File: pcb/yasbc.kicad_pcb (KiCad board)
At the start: 4 copper layers, 207 parts, among them J1 USB TTY, J10 BOOT, J11 AudioJack3, J12 1V5, J13 VDDR, J14 3V3, J15 1V2, J2 ESP32 IO, J3 TTY_UART, J4 USB DEV, J5 Micro_SD_Card, J6 USB HOST, J7 GPIO, J9 SSD1306, Q1 AO3401A, Q2 AO3401A, U1 BCT2028, U2 BCT2028, U3 ESP32-WROOM-32, U4 Allwinner_A13, U5 CH340E, U6 TD6810, U7 SE5120, U8 K4B4G1646E, U9 MPU-6050, Y1 24M

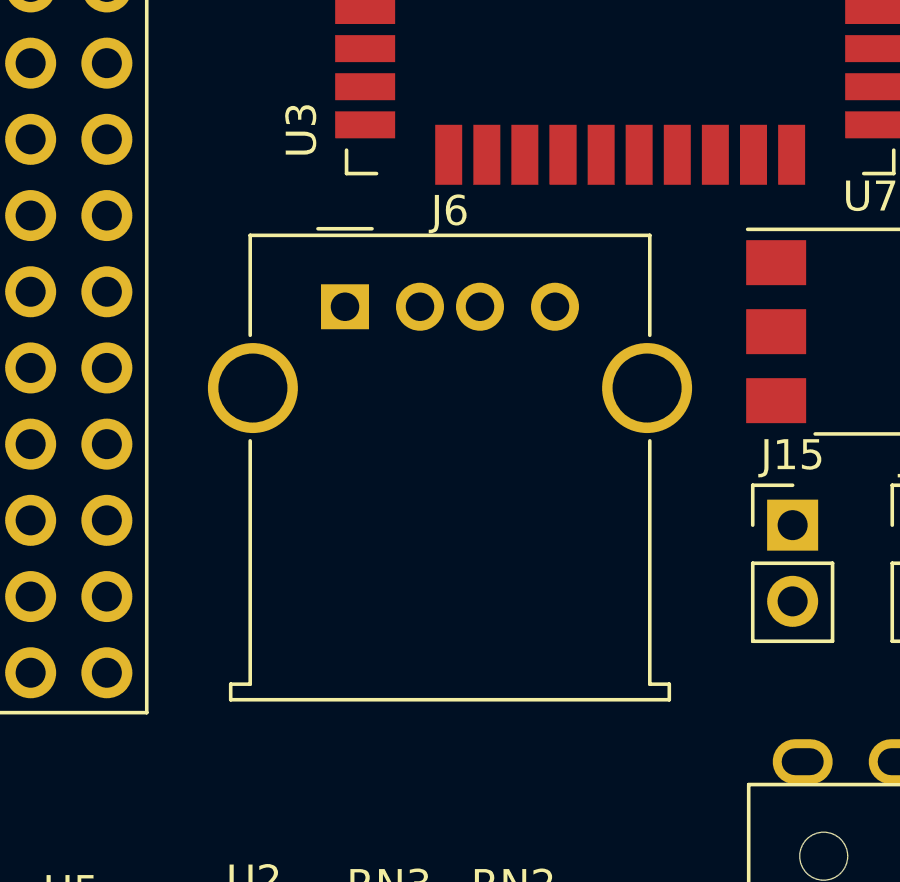
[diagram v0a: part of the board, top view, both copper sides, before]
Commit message: Added USB connector datasheets and footprints
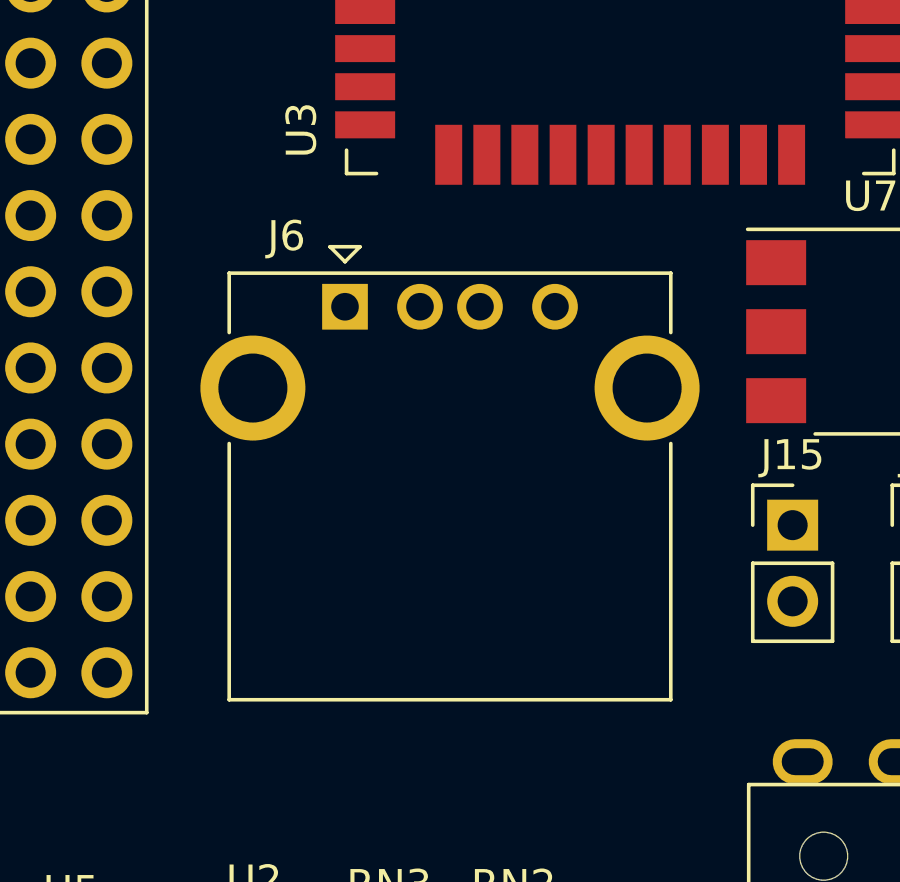
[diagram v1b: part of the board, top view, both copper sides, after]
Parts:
- J6: footprint Connector_USB:USB_A_Molex_67643_Horizontal -> Connector_USB:USB_A_CONNFLY_DS1095-WNR0

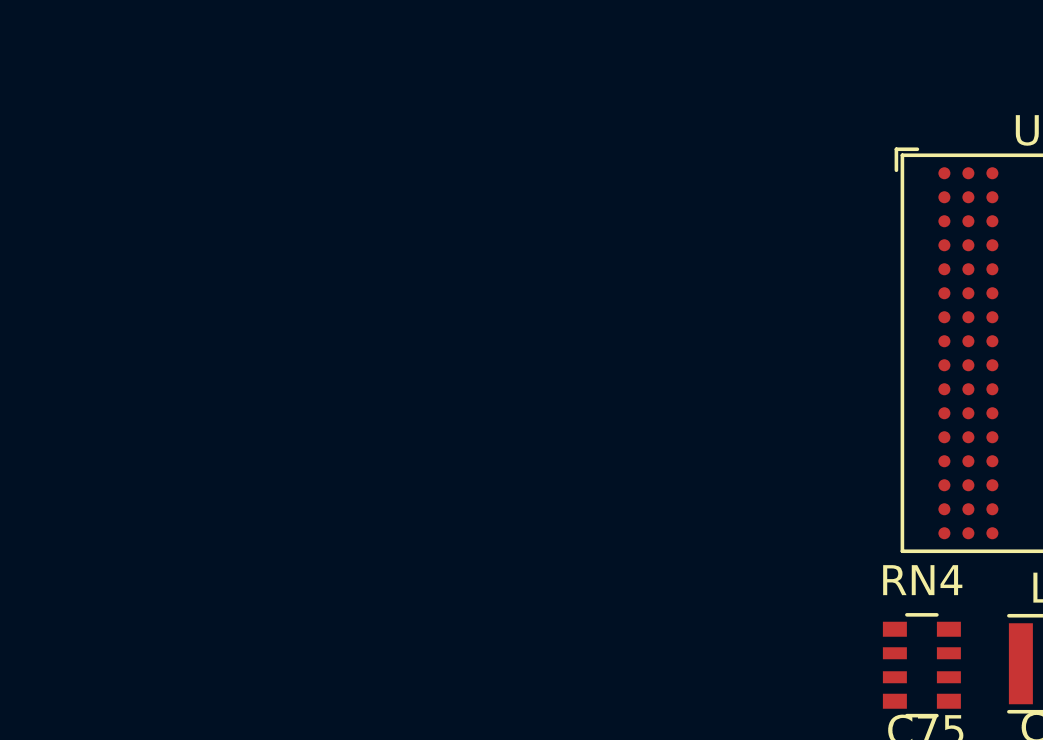
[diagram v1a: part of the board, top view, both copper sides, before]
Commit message: Added Reset and 5Way switch datasheets and footprints
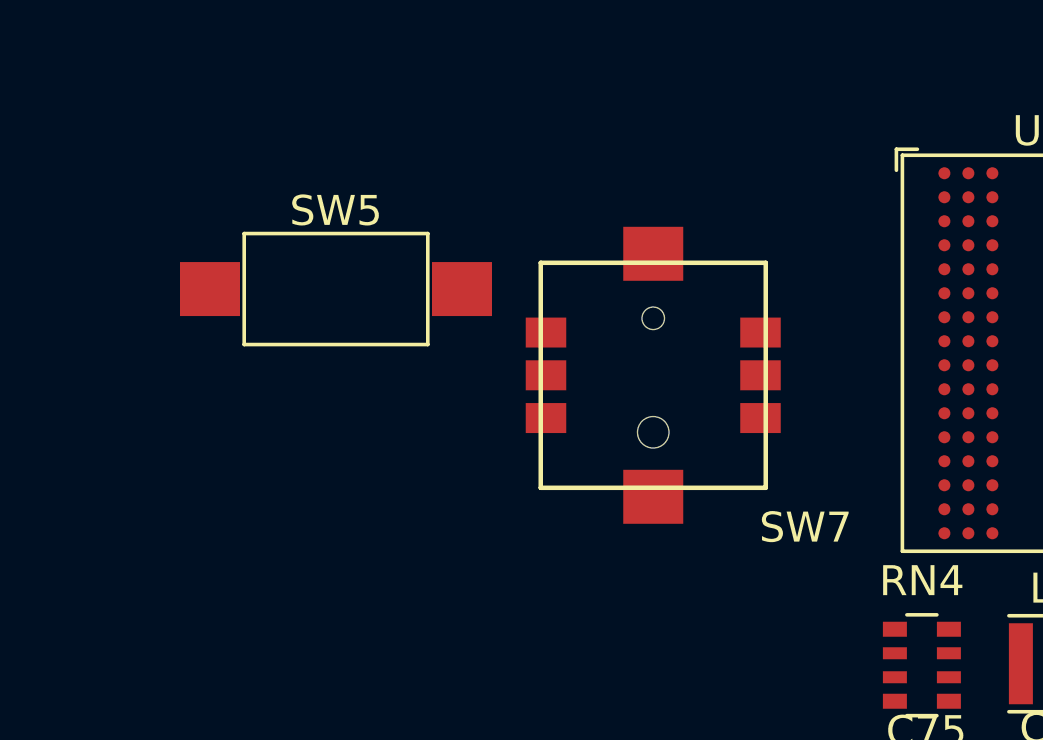
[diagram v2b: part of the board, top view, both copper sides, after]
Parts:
- added SW5: RESET, yasbc:HYP-1TS002B-2500-4300-CT, F.Cu at (-37.9, -30.6)
- added SW7: SW_5WAY, yasbc:Switches_ALPS-SKRHAAE010, F.Cu at (-27.3, -27.8)

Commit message: Added SPDT datasheets and footprints
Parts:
- added SW1: SW_SPDT, yasbc:SS-12D10, F.Cu at (38.8, -31.3)
- added SW2: SW_SPDT, yasbc:SS-12D10, F.Cu at (38.8, -23.2)
- added SW3: SW_SPDT, yasbc:SS-12D10, F.Cu at (53.1, -31.3)
- added SW4: SW_SPDT, yasbc:SS-12D10, F.Cu at (53.1, -23.2)

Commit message: Worked on layout
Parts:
- removed C46: 0.1u, Capacitor_SMD:C_0603_1608Metric
- removed J3: TTY_UART, Connector_PinHeader_2.54mm:PinHeader_1x03_P2.54mm_Vertical
- added TP1: TX, TestPoint:TestPoint_Pad_D2.0mm, F.Cu at (85.0, 121.5)
- added TP2: RX, TestPoint:TestPoint_Pad_D2.0mm, F.Cu at (85.0, 126.2)
- added TP3: GND, TestPoint:TestPoint_Pad_D2.0mm, F.Cu at (85.0, 131.0)
- C10, C11, C13, C15, C16, C18, C19, C20, C23, C24, C25, C28, C3, C30, C34, C35, C36, C37, C38, C39, C4, C41, C42, C43, C45, C47, C5, C50, C51, C53, C54, C56, C57, C58, C59, C8, C9, R11, R3, R4, R9, U3: moved to B.Cu
- C77, C78, C80, C81, C82, C83, C84, C85, C86, C87, C89, C90, C92, C93, C94, C97, C98, C99: footprint Capacitor_SMD:C_0603_1608Metric -> Capacitor_SMD:C_0402_1005Metric
- moved J15 350.8 mm to (264.3, 152.5), turned to 270 degrees
- moved U2 328.4 mm to (226.6, 156.6)
- moved U7 327.1 mm to (251.0, 123.2)
- moved L1 325.7 mm to (261.1, 156.3), turned to 90 degrees
- moved U6 324.1 mm to (265.5, 156.3)
- moved C55 317.0 mm to (258.3, 156.3), turned to 270 degrees
- moved J13 316.2 mm to (230.4, 152.6), turned to 270 degrees
- moved J12 315.2 mm to (247.8, 152.6), turned to 270 degrees
- moved C29 312.7 mm to (265.1, 159.1), turned to 180 degrees
- moved U3 312.5 mm to (237.4, 79.6), turned to 180 degrees
- moved U1 310.1 mm to (244.0, 156.6)
- moved R10 308.9 mm to (270.5, 156.3), turned to 270 degrees
- moved C32 308.8 mm to (268.7, 156.3), turned to 270 degrees
- moved C21 307.1 mm to (247.8, 157.6)
- moved C6 303.5 mm to (244.0, 159.6), turned to 180 degrees
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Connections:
- RN3 pad 1: /LED1 -> /LED3
- RN3 pad 2: /LED2 -> /LED1
- RN3 pad 3: /LED3 -> /LED2
- RN3 pad 6: Net-(D3-Pad2) -> Net-(D2-Pad2)
- RN3 pad 7: Net-(D2-Pad2) -> Net-(D1-Pad2)
- RN3 pad 8: Net-(D1-Pad2) -> Net-(D3-Pad2)
- RN4 pad 1: /LED5 -> Net-(D6-Pad2)
- RN4 pad 2: /LED6 -> Net-(D8-Pad2)
- RN4 pad 3: /LED7 -> Net-(D7-Pad2)
- RN4 pad 4: /LED8 -> Net-(D5-Pad2)
- RN4 pad 5: Net-(D8-Pad2) -> /LED5
- RN4 pad 6: Net-(D7-Pad2) -> /LED7
- RN4 pad 7: Net-(D6-Pad2) -> /LED8
- RN4 pad 8: Net-(D5-Pad2) -> /LED6
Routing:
- net Net-(J11-PadS): track 0.00 -> 18.8 mm
- net GND: track 0.00 -> 17.0 mm, vias 0 -> 19
- net VBUS: track 0.00 -> 16.5 mm
- net Net-(J11-PadT): track 0.00 -> 13.6 mm
- net Net-(C55-Pad1): track 0.00 -> 11.3 mm
- net +3V3: track 0.00 -> 10.9 mm
- net Net-(D5-Pad2): track 0.00 -> 10.4 mm
- net Net-(D4-Pad2): track 0.00 -> 10.3 mm
- net Net-(J11-PadR): track 0.00 -> 9.85 mm
- net Net-(J1-PadA7): track 0.00 -> 9.77 mm
- net Net-(J1-PadA6): track 0.00 -> 7.90 mm
- net Net-(J4-PadA5): track 0.00 -> 7.84 mm
- net Net-(J1-PadA5): track 0.00 -> 7.84 mm
- net Net-(J1-PadB5): track 0.00 -> 7.59 mm
- net Net-(J4-PadB5): track 0.00 -> 7.59 mm
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
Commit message: Added boost reg for OLED and new inductors
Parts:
- added C106: 10u, Capacitor_SMD:C_0603_1608Metric, F.Cu at (206.0, 158.0)
- added C46: 10u, Capacitor_SMD:C_0603_1608Metric, F.Cu at (202.0, 158.0)
- added L2: 4.7u, Inductor_SMD:L_0805_2012Metric_Pad1.15x1.40mm_HandSolder, F.Cu at (207.2, 154.4)
- added R65: 10K, Resistor_SMD:R_0603_1608Metric, F.Cu at (211.5, 153.3)
- added R66: 200K, Resistor_SMD:R_0603_1608Metric, F.Cu at (210.0, 158.0)
- added U10: MT3608, Package_TO_SOT_SMD:SOT-23-6, F.Cu at (202.4, 154.4)
- L1: footprint yasbc:Inductor_SMD_3x3mm -> Inductor_SMD:L_1008_2520Metric
- moved C64 235.2 mm to (159.9, 157.3)
- moved R63 232.0 mm to (155.0, 160.8)
- moved R56 228.8 mm to (154.6, 157.0)
- moved C65 227.7 mm to (158.2, 152.0)
- moved R55 216.4 mm to (149.0, 147.0)
- moved R12 214.7 mm to (149.0, 150.8)
- moved R54 214.4 mm to (144.0, 150.2)
- moved C103 211.8 mm to (152.8, 150.8)
- moved R59 211.4 mm to (144.0, 146.0)
- moved C66 208.4 mm to (155.6, 145.7)
- moved C68 208.4 mm to (159.6, 143.2)
- moved D1 135.5 mm to (110.8, 147.6)
- moved D2 135.5 mm to (112.8, 147.6)
- moved D3 135.5 mm to (114.8, 147.6)
- moved D4 135.5 mm to (116.8, 147.6)
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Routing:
- net GND: track 17.0 -> 26.9 mm, vias 19 -> 11
- net Net-(C26-Pad1): track 0.00 -> 3.12 mm
- net VBUS: track 16.5 -> 14.1 mm
- net Net-(C6-Pad1): track 1.95 -> 4.13 mm
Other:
- board text added: "OLED"

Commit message: Added new OLED, worked on sch & pcb
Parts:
- removed the C104 at (182.7, 72.6)
- removed C106: 10u, Capacitor_SMD:C_0603_1608Metric
- removed the C26 at (247.8, 155.6)
- removed the C46 at (202.0, 158.0)
- removed the C55 at (258.2, 155.9)
- removed the C63 at (125.0, 77.6)
- removed the C70 at (120.1, 28.5)
- removed the C71 at (122.6, 28.5)
- removed the C95 at (179.5, 71.0)
- removed the C96 at (182.7, 71.0)
- removed the J2 at (-43.4, -9.74)
- removed the J7 at (-80.1, -34.2)
- removed the R16 at (-17.9, 14.7)
- removed the R17 at (6.98, -10.0)
- removed the R18 at (-6.70, 3.79)
- removed the R19 at (15.0, -17.6)
- removed the R23 at (-10.7, 1.28)
- removed the R24 at (10.6, -20.1)
- removed the R25 at (-25.9, 17.2)
- removed the R26 at (-1.08, -7.74)
- removed the R29 at (-3.77, 6.30)
- removed the R30 at (-13.9, 17.2)
- removed the R31 at (-8.77, 12.2)
- removed the R35 at (-18.1, 22.2)
- removed the R36 at (-4.76, 8.81)
- removed R40, R41: 22, Resistor_SMD:R_0603_1608Metric
- removed R42, R51: 240 1%, Resistor_SMD:R_0603_1608Metric
- removed R43, R44, R52, R53: 2K, Resistor_SMD:R_0603_1608Metric
- removed R45: 47K, Resistor_SMD:R_0603_1608Metric
- removed R47, R48: 100, Resistor_SMD:R_0603_1608Metric
- removed R57, R58: 5.1K, Resistor_SMD:R_0603_1608Metric
- removed the U10 at (202.4, 154.4)
- added C100: 0.1u, Capacitor_SMD:C_0603_1608Metric, F.Cu at (143.3, 122.2)
- added C101: 0.1u, Capacitor_SMD:C_0603_1608Metric, F.Cu at (140.1, 120.6)
- added C102: 0.1u, Capacitor_SMD:C_0603_1608Metric, F.Cu at (143.3, 120.6)
- added C28: 0.1u, Capacitor_SMD:C_0603_1608Metric, F.Cu at (247.5, 155.5)
- added C48: 10u, Capacitor_SMD:C_0603_1608Metric, F.Cu at (259.5, 155.9)
- added C65: 10u, Capacitor_SMD:C_0603_1608Metric, F.Cu at (198.0, 154.4)
- added C66: 0.1u, Capacitor_SMD:C_0603_1608Metric, F.Cu at (121.8, 77.6)
- added D1: D_Schottky, Diode_SMD:D_SOD-323, F.Cu at (198.9, 151.8)
- added U9: K4B4G1646E, Package_BGA:BGA-96_9.0x13.0mm_Layout2x3x16_P0.8mm, F.Cu at (106.6, 100.7)
- C62: value 0.1u -> 10u
- C67: value 10u -> 0.1u
- C72: value 1u -> 10u
- J11: renamed from J9; value SSD1306 -> SSD1309; footprint yasbc:SSD1306 -> yasbc:SSD1309
- R20, R37: value 22 -> 240 1%
- R21, R22, R38, R39: value 22 -> 2K
- R27, R28: value 22 -> 5.1K
- R31: renamed from R46; value 400K -> 960K
- R32, R33: value 22 -> 100
- R34: value 22 -> 47K
- U8: value K4B4G1646E -> MT3608; footprint Package_BGA:BGA-96_9.0x13.0mm_Layout2x3x16_P0.8mm -> Package_TO_SOT_SMD:SOT-23-6
- moved R39 190.1 mm to (143.3, 119.0)
- moved R37 183.6 mm to (140.1, 122.2)
- moved R38 182.2 mm to (140.1, 119.0)
- moved C67 156.6 mm to (125.0, 77.6)
- moved R22 150.6 mm to (125.0, 76.0)
- moved R21 144.0 mm to (121.8, 76.0)
- moved R20 142.6 mm to (125.0, 74.4)
- moved C62 111.7 mm to (205.1, 152.0), turned to 270 degrees
- moved C72 110.2 mm to (15.6, 16.4), turned to 0 degrees
- moved U8 86.0 mm to (202.4, 154.4)
- moved C82 67.7 mm to (122.3, 119.8)
- moved C83 67.7 mm to (122.3, 121.4)
- moved C91 67.7 mm to (122.3, 123.0)
- moved C97 67.7 mm to (122.3, 124.6)
- moved C103 67.7 mm to (131.9, 124.6)
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- renumbered C97 to C103, C98 to C104, C99 to C105, C15 to C14, C16 to C15, C17 to C16, C18 to C17, C19 to C18, C20 to C19, C14 to C20, C100 to C23, C23 to C24, C24 to C25, C25 to C26, C101 to C27, C27 to C29, C102 to C30, C33 to C31, C28 to C32, C29 to C33, C30 to C34, C31 to C35, C32 to C36, C34 to C37, C35 to C38, C36 to C39, C37 to C40, C38 to C41, C39 to C42, C40 to C43, C41 to C44, C42 to C45, C43 to C46, C44 to C47, C45 to C49, C47 to C50, C48 to C51, C49 to C52, C50 to C53, C51 to C54, C52 to C55, C53 to C56, C54 to C57, C56 to C58, C57 to C59, C58 to C60, C59 to C61, C60 to C63, C61 to C64, C103 to C68, C64 to C69, C65 to C70, C66 to C71, C69 to C73, C68 to C74, C73 to C78, C74 to C79, C75 to C80, C76 to C81, C77 to C82, C78 to C83, C79 to C84, C80 to C85, C81 to C86, C82 to C87, C83 to C88, C84 to C89, C85 to C90, C86 to C91, C87 to C92, C88 to C93, C89 to C94, C90 to C95, C91 to C96, C92 to C97, C93 to C98, C94 to C99, D3 to D2, D1 to D3, D2 to D4, D4 to D5, D8 to D7, D7 to D8, D5 to D9, J10 to J1, J6 to J10, J1 to J2, J11 to J3, J12 to J4, J13 to J5, J14 to J6, J15 to J7, J4 to J8, J5 to J9, R61 to R10, R62 to R11, R9 to R12, R10 to R13, R11 to R14, R13 to R15, R14 to R16, R15 to R17, R66 to R18, R65 to R19, R12 to R23, R54 to R24, R55 to R25, R56 to R26, R59 to R29, R8 to R3, R63 to R30, R49 to R35, R50 to R36, R3 to R4, R4 to R5, R5 to R6, R60 to R8, R6 to R9, RN2 to RN1, RN3 to RN2, RN4 to RN3, RN5 to RN4, SW5 to SW1, SW4 to SW2, SW2 to SW4, SW1 to SW5, SW7 to SW6, U9 to U10
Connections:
- net /USB_DEV_DM renamed /USB_DEV_D-
- net /USB_DEV_DP renamed /USB_DEV_D+
- net /USB_HOST_DM renamed /USB_HOST_D-
- net /USB_HOST_DP renamed /USB_HOST_D+
- C62 pad 1: +1V5 -> VBUS
- C62 pad 2: Net-(C62-Pad2) -> GND
- C67 pad 1: /SW_CENTER -> Net-(C66-Pad2)
- C72 pad 1: +3V3 -> /SW_CENTER
- C73 pad 1: Net-(C69-Pad1) -> Net-(C73-Pad1)
- C79 pad 1: Net-(C74-Pad1) -> +12V
- J11 pad 10: GND -> Net-(J11-Pad10)
- J11 pad 11: GND -> /OLED_SDIN
- J11 pad 12: GND -> /OLED_SCLK
- J11 pad 13: /OLED_CS -> GND
- J11 pad 14: /OLED_RES -> GND
- J11 pad 16: GND -> /OLED_RES
- J11 pad 17: GND -> /OLED_CS
- J11 pad 18: /OLED_SCLK -> Net-(J11-Pad18)
- J11 pad 19: /OLED_SDIN -> GND
- J11 pad 2: Net-(C70-Pad1) -> +12V
- J11 pad 20: Net-(J9-Pad20) -> GND
- J11 pad 21: GND -> +3V3
- J11 pad 22: GND -> Net-(J11-Pad22)
- J11 pad 23: GND -> Net-(J11-Pad23)
- J11 pad 24: GND -> Net-(J11-Pad24)
- J11 pad 25: GND -> Net-(J11-Pad25)
- J11 pad 26: Net-(J9-Pad26) -> Net-(J11-Pad26)
- J11 pad 27: Net-(C69-Pad1) -> Net-(J11-Pad27)
- J11 pad 28: Net-(C74-Pad1) -> Net-(J11-Pad28)
- J11 pad 29: GND -> Net-(J11-Pad29)
- J11 pad 3: Net-(C70-Pad2) -> Net-(C73-Pad1)
- J11 pad 4: Net-(C71-Pad1) -> Net-(J11-Pad4)
- J11 pad 5: Net-(C71-Pad2) -> GND
- J11 pad 6: +3V3 -> GND
- J11 pad 7: Net-(J9-Pad7) -> GND
- J11 pad 9: +3V3 -> GND
- L2 pad 2: Net-(D9-Pad2) (its old number) -> Net-(D1-Pad2)
- R18 pad 2: Net-(R65-Pad2) -> Net-(R18-Pad2)
- R19 pad 2: Net-(R65-Pad2) -> Net-(R18-Pad2)
- R20 pad 2: /DDR3_CKN -> GND
- R21 pad 1: Net-(R21-Pad1) -> +1V5
- R21 pad 2: /DDR3_CKE -> Net-(C66-Pad2)
- R22 pad 1: Net-(R22-Pad1) -> Net-(C66-Pad2)
- R22 pad 2: /DDR3_RST -> GND
- R24 pad 1: Net-(R54-Pad1) -> Net-(R24-Pad1)
- R25 pad 1: Net-(R55-Pad1) -> Net-(R25-Pad1)
- R27 pad 1: Net-(R27-Pad1) -> Net-(R24-Pad1)
- R27 pad 2: /DDR3_A0 -> /SW_R2R
- R28 pad 1: Net-(R28-Pad1) -> Net-(R25-Pad1)
- R28 pad 2: /DDR3_A1 -> Net-(R24-Pad1)
- R29 pad 2: Net-(R55-Pad1) -> Net-(R25-Pad1)
- R31 pad 1: Net-(J9-Pad26) -> Net-(J11-Pad4)
- R32 pad 2: /DDR3_A5 -> /TTY_TX
- R33 pad 2: /DDR3_A6 -> /TTY_RX
- R34 pad 1: Net-(R34-Pad1) -> /SW_LEFT
- R34 pad 2: /DDR3_A7 -> GND
- R37 pad 2: /DDR3_A10 -> GND
- R38 pad 1: Net-(R38-Pad1) -> VDDR
- R38 pad 2: /DDR3_A11 -> Net-(C101-Pad2)
- R39 pad 1: Net-(R39-Pad1) -> Net-(C101-Pad2)
- R39 pad 2: /DDR3_A12 -> GND
- RN4 pad 5: /SW_DOWN -> /SW_CENTER
- RN4 pad 6: /SW_CENTER -> /SW_RIGHT
- RN4 pad 7: /SW_RIGHT -> /SW_UP
- RN4 pad 8: /SW_UP -> /SW_DOWN
- U3 pad 10: /IO25 -> Net-(U3-Pad10)
- U3 pad 11: /IO26 -> Net-(U3-Pad11)
- U3 pad 12: /IO27 -> Net-(U3-Pad12)
- U3 pad 27: /IO16 -> Net-(U3-Pad27)
- U3 pad 28: /IO17 -> Net-(U3-Pad28)
- U3 pad 29: /IO5 -> Net-(U3-Pad29)
- U3 pad 30: /IO18 -> Net-(U3-Pad30)
- U3 pad 33: /IO21 -> Net-(U3-Pad33)
- U3 pad 37: /IO23 -> Net-(U3-Pad37)
- U3 pad 6: /IO34 -> Net-(U3-Pad6)
- U3 pad 7: /IO35 -> Net-(U3-Pad7)
- U3 pad 8: /IO32 -> Net-(U3-Pad8)
- U3 pad 9: /IO33 -> Net-(U3-Pad9)
- U4 pad 114: /CSI_PCLK -> Net-(U4-Pad114)
- U4 pad 115: /CSI_MCLK -> Net-(U4-Pad115)
- U4 pad 116: /CSI_HSYNC -> Net-(U4-Pad116)
- U4 pad 117: /CSI_VSYNC -> Net-(U4-Pad117)
- U4 pad 118: /CSI_D0 -> Net-(U4-Pad118)
- U4 pad 119: /CSI_D1 -> Net-(U4-Pad119)
- U4 pad 120: /CSI_D2 -> Net-(U4-Pad120)
- U4 pad 121: /CSI_D3 -> Net-(U4-Pad121)
- U4 pad 122: /CSI_D4 -> Net-(U4-Pad122)
- U4 pad 123: /CSI_D5 -> Net-(U4-Pad123)
- U4 pad 124: /CSI_D6 -> Net-(U4-Pad124)
- U4 pad 125: /CSI_D7 -> Net-(U4-Pad125)
- U4 pad 126: /LCD_VSYNC -> Net-(U4-Pad126)
- U4 pad 127: /LCD_HSYNC -> Net-(U4-Pad127)
- U4 pad 128: /LCD_DE -> Net-(U4-Pad128)
- U4 pad 129: /LCD_CLK -> Net-(U4-Pad129)
- U4 pad 130: /LCD_D23 -> Net-(U4-Pad130)
- U4 pad 131: /LCD_D22 -> Net-(U4-Pad131)
- U4 pad 132: /LCD_D21 -> Net-(U4-Pad132)
- U4 pad 133: /LCD_D20 -> Net-(U4-Pad133)
- U4 pad 134: /LCD_D19 -> Net-(U4-Pad134)
- U4 pad 135: /LCD_D18 -> Net-(U4-Pad135)
- U4 pad 136: /LCD_D15 -> Net-(U4-Pad136)
- U4 pad 137: /LCD_D14 -> Net-(U4-Pad137)
- U4 pad 138: /LCD_D13 -> Net-(U4-Pad138)
- U4 pad 139: /LCD_D12 -> Net-(U4-Pad139)
- U4 pad 140: /LCD_D11 -> Net-(U4-Pad140)
- U4 pad 141: /LCD_D10 -> Net-(U4-Pad141)
- U4 pad 143: /LCD_D7 -> Net-(U4-Pad143)
- U4 pad 144: /LCD_D6 -> Net-(U4-Pad144)
- U4 pad 145: /LCD_D5 -> Net-(U4-Pad145)
- U4 pad 146: /LCD_D4 -> Net-(U4-Pad146)
- U4 pad 147: /LCD_D3 -> Net-(U4-Pad147)
- U4 pad 148: /LCD_D2 -> Net-(U4-Pad148)
- U4 pad 151: Net-(R48-Pad1) -> Net-(R33-Pad1)
- U4 pad 152: Net-(R47-Pad1) -> Net-(R32-Pad1)
- U4 pad 17: Net-(R42-Pad1) -> Net-(R20-Pad1)
- U4 pad 18: Net-(C62-Pad2) -> Net-(C66-Pad2)
- U4 pad 31: /DDR3_DQS0 -> /DDR3_DQS0+
- U4 pad 32: /DDR3_DQS0N -> /DDR3_DQS0-
- U4 pad 33: /DDR3_DQS1 -> /DDR3_DQS1+
- U4 pad 34: /DDR3_DQS1N -> /DDR3_DQS1-
- U4 pad 45: Net-(R19-Pad1) -> /DDR3_CK+
- U4 pad 46: Net-(R20-Pad1) -> /DDR3_CK-
- U4 pad 47: Net-(R21-Pad1) -> /DDR3_CKE
- U4 pad 48: Net-(R37-Pad1) -> /DDR3_A10
- U4 pad 49: Net-(R17-Pad1) -> /DDR3_BA1
- U4 pad 50: Net-(R39-Pad1) -> /DDR3_A12
- U4 pad 51: Net-(R31-Pad1) -> /DDR3_A4
- U4 pad 52: Net-(R28-Pad1) -> /DDR3_A1
- U4 pad 54: Net-(R33-Pad1) -> /DDR3_A6
- U4 pad 55: Net-(R35-Pad1) -> /DDR3_A8
- U4 pad 56: Net-(R38-Pad1) -> /DDR3_A11
- U4 pad 57: Net-(R41-Pad1) -> /DDR3_A14
- U4 pad 58: Net-(R24-Pad1) -> /DDR3_RAS
- U4 pad 59: Net-(R23-Pad1) -> /DDR3_CAS
- U4 pad 60: Net-(R25-Pad1) -> /DDR3_WE
- U4 pad 61: Net-(R18-Pad1) -> /DDR3_BA2
- U4 pad 63: Net-(R16-Pad1) -> /DDR3_BA0
- U4 pad 64: Net-(R27-Pad1) -> /DDR3_A0
- U4 pad 65: Net-(R30-Pad1) -> /DDR3_A3
- U4 pad 66: Net-(R29-Pad1) -> /DDR3_A2
- U4 pad 67: Net-(R32-Pad1) -> /DDR3_A5
- U4 pad 68: Net-(R40-Pad1) -> /DDR3_A13
- U4 pad 69: Net-(R36-Pad1) -> /DDR3_A9
- U4 pad 70: Net-(R22-Pad1) -> /DDR3_RST
- U4 pad 71: Net-(R34-Pad1) -> /DDR3_A7
- U4 pad 72: Net-(R26-Pad1) (its old number) -> /DDR3_ODT
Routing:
- net GND: track 26.9 -> 46.4 mm, vias 11 -> 6
- net /DDR3_D5: track 0.00 -> 10.4 mm
- net /DDR3_D7: track 0.00 -> 9.78 mm
- net /DDR3_D4: track 0.00 -> 9.16 mm
- net /DDR3_D6: track 0.00 -> 8.99 mm
- net /DDR3_D3: track 0.00 -> 8.72 mm
- net /DDR3_DQS0-: track 0.00 -> 8.49 mm
- net /DDR3_D1: track 0.00 -> 8.12 mm
- net /DDR3_D2: track 0.00 -> 8.11 mm
- net /DDR3_DQS0+: track 0.00 -> 7.68 mm
- net VBUS: track 14.1 -> 21.7 mm
- net /DDR3_DM0: track 0.00 -> 7.33 mm
- net /DDR3_D0: track 0.00 -> 6.91 mm
- net Net-(C95-Pad2): track 6.44 -> 0.00 mm
- net Net-(C101-Pad2): track 0.00 -> 6.44 mm
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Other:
- net class Default: clearance 0.1524 -> 0.1016; via_dia 0.4064 -> 0.4572
- net class HighSpeed added: clearance 0.1016, trace_width 0.2032, via_dia 0.4572, via_drill 0.2032
- rule trace_clearance: 0.1524 -> 0.1016
- rule trace_min: 0.127 -> 0.1016
- rule via_min_size: 0.4 -> 0.45
- board text removed: "OLED"

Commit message: Reduced to one +1V5 LDO
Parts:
- removed the C2 at (223.1, 155.6)
- removed the C22 at (230.1, 157.7)
- removed the C29 at (230.1, 155.5)
- removed the C7 at (226.6, 159.3)
- removed the J5 at (230.4, 152.6)
- removed the R2 at (223.1, 157.6)
- removed the U2 at (226.6, 156.6)
- C1: value 0.1u -> 1u
- C25: renamed from C28; value 0.1u -> 1u
- renumbered C12 to C10, C13 to C11, C14 to C12, C15 to C13, C16 to C14, C17 to C15, C18 to C16, C19 to C17, C20 to C18, C21 to C19, C3 to C2, C23 to C20, C24 to C21, C25 to C22, C26 to C23, C27 to C24, C30 to C26, C31 to C27, C32 to C28, C33 to C29, C4 to C3, C34 to C30, C35 to C31, C36 to C32, C37 to C33, C38 to C34, C39 to C35, C40 to C36, C41 to C37, C42 to C38, C43 to C39, C5 to C4, C44 to C40, C45 to C41, C46 to C42, C47 to C43, C48 to C44, C49 to C45, C50 to C46, C51 to C47, C52 to C48, C53 to C49, C6 to C5, C54 to C50, C55 to C51, C56 to C52, C57 to C53, C58 to C54, C59 to C55, C60 to C56, C61 to C57, C62 to C58, C63 to C59, C8 to C6, C64 to C60, C65 to C61, C66 to C62, C67 to C63, C68 to C64, C69 to C65, C70 to C66, C71 to C67, C72 to C68, C74 to C69, C9 to C7, C80 to C70, C82 to C71, C81 to C72, C83 to C73, C84 to C74, C73 to C75, C85 to C76, C86 to C77, C79 to C78, C78 to C79, C10 to C8, C87 to C80, C88 to C81, C89 to C82, C90 to C83, C91 to C84, C92 to C85, C94 to C86, C93 to C87, C95 to C88, C96 to C89, C11 to C9, C97 to C90, C98 to C91, C99 to C92, C100 to C93, C101 to C94, C102 to C95, C103 to C96, C104 to C97, C105 to C98, J11 to J10, J6 to J5, J7 to J6, J8 to J7, J9 to J8, J10 to J9, R11 to R10, R12 to R11, R13 to R12, R14 to R13, R15 to R14, R16 to R15, R17 to R16, R18 to R17, R19 to R18, R20 to R19, R3 to R2, R21 to R20, R22 to R21, R23 to R22, R24 to R23, R25 to R24, R26 to R25, R27 to R26, R28 to R27, R29 to R28, R30 to R29, R4 to R3, R32 to R30, R33 to R31, R34 to R32, R35 to R33, R36 to R34, R31 to R35, R37 to R36, R38 to R37, R39 to R38, R5 to R4, R6 to R5, R7 to R6, R8 to R7, R9 to R8, R10 to R9, U3 to U2, U4 to U3, U5 to U4, U6 to U5, U7 to U6, U8 to U7, U9 to U8, U10 to U9
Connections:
- C70 pad 1: VDDR -> +1V5
- C71 pad 1: VDDR -> +1V5
- C73 pad 1: VDDR -> +1V5
- C76 pad 1: VDDR -> +1V5
- C77 pad 1: VDDR -> +1V5
- C80 pad 1: VDDR -> +1V5
- C81 pad 1: VDDR -> +1V5
- C82 pad 1: VDDR -> +1V5
- C83 pad 1: VDDR -> +1V5
- C84 pad 1: VDDR -> +1V5
- C85 pad 1: VDDR -> +1V5
- C86 pad 1: VDDR -> +1V5
- C88 pad 1: VDDR -> +1V5
- C90 pad 1: VDDR -> +1V5
- C91 pad 1: VDDR -> +1V5
- C92 pad 1: VDDR -> +1V5
- C94 pad 1: VDDR -> +1V5
- C96 pad 1: VDDR -> +1V5
- C97 pad 1: VDDR -> +1V5
- C98 pad 1: VDDR -> +1V5
- R37 pad 1: VDDR -> +1V5
- U8 pad A1: VDDR -> +1V5
- U8 pad A8: VDDR -> +1V5
- U8 pad B2: VDDR -> +1V5
- U8 pad C1: VDDR -> +1V5
- U8 pad C9: VDDR -> +1V5
- U8 pad D2: VDDR -> +1V5
- U8 pad D9: VDDR -> +1V5
- U8 pad E9: VDDR -> +1V5
- U8 pad F1: VDDR -> +1V5
- U8 pad G7: VDDR -> +1V5
- U8 pad H2: VDDR -> +1V5
- U8 pad H9: VDDR -> +1V5
- U8 pad K2: VDDR -> +1V5
- U8 pad K8: VDDR -> +1V5
- U8 pad N1: VDDR -> +1V5
- U8 pad N9: VDDR -> +1V5
- U8 pad R1: VDDR -> +1V5
- U8 pad R9: VDDR -> +1V5
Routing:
- net GND: track 46.4 -> 38.8 mm
- net VBUS: track 21.7 -> 16.9 mm
- net Net-(C29-Pad1): track 4.54 -> 0.00 mm
- net Net-(C7-Pad1): track 3.48 -> 0.00 mm
- net Net-(C22-Pad1): track 1.65 -> 0.00 mm
- net VDDR: track 1.62 -> 0.00 mm
- net +1V5: track 1.62 -> 3.24 mm

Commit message: Worked on layout
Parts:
- C45, C53, C6, R3, R4, U2: moved to F.Cu
- C75, C78, C79, J10, R35: moved to B.Cu
- moved R30 194.7 mm to (178.6, 131.3)
- moved C68 194.7 mm to (174.6, 128.8)
- moved R26 194.7 mm to (174.6, 131.3)
- moved R27 194.7 mm to (178.6, 128.8)
- moved R31 194.7 mm to (182.6, 128.8)
- moved R32 194.7 mm to (182.6, 131.3)
- moved R3 140.7 mm to (134.8, -2.25)
- moved J8 140.1 mm to (52.8, 31.4), turned to 270 degrees
- moved R15 139.1 mm to (168.9, 53.8), turned to 0 degrees
- moved C53 137.7 mm to (136.6, -5.45)
- moved C6 137.7 mm to (136.6, -2.25)
- moved R14 137.0 mm to (59.8, 36.4), turned to 180 degrees
- moved C45 134.7 mm to (138.3, -5.45)
- moved R4 134.7 mm to (138.3, -2.25)
- moved RN1 134.4 mm to (59.8, 33.6), turned to 180 degrees
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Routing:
- net GND: track 38.8 -> 44.1 mm, vias 6 -> 7
- net /DDR3_D4: track 9.16 -> 13.4 mm
- net +1V5: track 3.24 -> 7.11 mm, vias 0 -> 2
- net /DDR3_D10: track 6.14 -> 3.41 mm
- net /DDR3_DM0: track 7.33 -> 5.00 mm, vias 0 -> 1
- net /DDR3_D3: track 8.72 -> 6.46 mm
- net /DDR3_D1: track 8.12 -> 5.94 mm, vias 0 -> 1
- net /DDR3_D2: track 8.11 -> 5.95 mm, vias 0 -> 1
- net /DDR3_D12: track 3.69 -> 1.63 mm
- net /DDR3_D14: track 4.64 -> 2.60 mm
- net /DDR3_DQS1+: track 5.56 -> 3.56 mm
- net /DDR3_D5: track 10.4 -> 8.41 mm
- net /DDR3_DM1: track 6.11 -> 4.20 mm, vias 0 -> 1
- net /DDR3_D15: track 3.54 -> 1.63 mm
- net /DDR3_D7: track 9.78 -> 7.93 mm
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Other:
- net class DDR3 added: clearance 0.3048, trace_width 0.1016, via_dia 0.4572, via_drill 0.2032
- net class HighSpeed removed
- board text added: "2.42" OLED"
